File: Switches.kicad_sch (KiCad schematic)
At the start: 26 parts, among them J3 INDICATOR_SWITCH_OUT

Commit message: r pt 2
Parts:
- IGN_SW1: Height 15.1 -> (none); Manufacturer_Name C & K COMPONENTS -> (none); Manufacturer_Part_Number RM103772BCB -> (none); Mouser Part Number 611-RM103772BCB -> (none); Mouser Price/Stock https://www.mouser.co.uk/ProductDetail/CK/RM103772BCB?qs=36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 -> (none)
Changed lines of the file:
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@@
 			)
 		)
-		(property "Datasheet" "~"
+		(property "Datasheet" "https://www.ckswitches.com/media/1349/arotary.pdf"
 			(at 213.36 55.88 0)
 			(effects
@@
 			)
 		)
-		(property "Height" "15.1"
+		(property "Height" ""
 			(at 229.87 443.18 0)
 			(effects
@@
 			)
 		)
-		(property "Mouser Part Number" "611-RM103772BCB"
+		(property "Mouser Part Number" ""
 			(at 229.87 543.18 0)
 			(effects
@@
 			)
 		)
-		(property "Mouser Price/Stock" "https://www.mouser.co.uk/ProductDetail/CK/RM103772BCB?qs=367PjNmvCmkgg4M2NDGHLA%3D%3D"
+		(property "Mouser Price/Stock" ""
 			(at 229.87 643.18 0)
 			(effects
@@
 			)
 		)
-		(property "Manufacturer_Name" "C & K COMPONENTS"
+		(property "Manufacturer_Name" ""
 			(at 229.87 743.18 0)
 			(effects
@@
 			)
 		)
-		(property "Manufacturer_Part_Number" "RM103772BCB"
+		(property "Manufacturer_Part_Number" ""
 			(at 229.87 843.18 0)
 			(effects

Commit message: Changed layout, added 3d models
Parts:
- CRUZ_EN_SW1, CRUZ_SET_SW1: footprint switched:SW_Butt_) -> Button_Switch_THT:SW_PUSH_6mm
- GR_SW1: footprint switched:SW_100_SP3T-Vertical -> switched:3posSlideToggle
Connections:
- net +12V: now also GR_SW1.1; no longer GR_SW1.2 (3)
- net FWD_SW: now also GR_SW1.2; no longer GR_SW1.1
- net REV_SW: now also GR_SW1.4; no longer GR_SW1.3 (4)
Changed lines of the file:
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@@
 			)
 		)
-		(property "Footprint" "switched:SW_100_SP3T-Vertical"
+		(property "Footprint" "switched:3posSlideToggle"
 			(at 154.94 38.1 0)
 			(effects
@@
 			)
 		)
-		(property "Datasheet" "~"
+		(property "Datasheet" "https://www.vimex.com/switches/techdocs/SS13F11-tech.pdf"
 			(at 168.91 57.15 0)
 			(effects
@@
 		(pin "2"
 		)
-		(pin "3"
+		(pin "4"
 		)
 		(pin "1"
@@
 			)
 		)
-		(property "Footprint" "switched:SW_Butt_)"
+		(property "Footprint" "Button_Switch_THT:SW_PUSH_6mm"
 			(at 49.53 110.49 0)
 			(effects
@@
 			)
 		)
-		(property "Footprint" "switched:SW_Butt_)"
+		(property "Footprint" "Button_Switch_THT:SW_PUSH_6mm"
 			(at 86.36 110.49 0)
 			(effects

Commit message: Some extra stuff and things
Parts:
- HZD_SW1: symbol Switch:SW_SPST -> Switch:SW_Push
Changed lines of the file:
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@@
 	)
 	(symbol
-		(lib_id "Switch:SW_SPST")
+		(lib_id "Switch:SW_Push")
 		(at 109.22 45.72 270)
 		(unit 1)
@@
 		)
 		(property "Footprint" "switched:SW_HAZARD"
-			(at 109.22 45.72 0)
+			(at 114.3 45.72 0)
 			(effects
 				(font
@@
 			)
 		)
-		(property "Datasheet" "https://www.digikey.com/en/products/detail/switch-components/TE1-1A-DC-1-AL/11493057"
-			(at 109.22 45.72 0)
+		(property "Datasheet" "https://www.mouser.com/datasheet/2/140/P200001-2487714.pdf"
+			(at 114.3 45.72 0)
 			(effects
 				(font
@@
 			)
 		)
-		(property "Description" "Single Pole Single Throw (SPST) switch"
+		(property "Description" "Push button switch, generic, two pins"
 			(at 109.22 45.72 0)
 			(effects

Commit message: Fixed stuff
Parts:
- GR_SW1: Link (none) -> https://www.amazon.com/Yohii-Position-Vertical-Switch-SS13F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
- HZD_SW1: footprint switched:SW_HAZARD -> switched:Toggle; P/N (none) -> JN2UEENAGX
- IGN_SW1: DigiKey Part Number (none) -> CKN9823-ND; Manufacturer_Part_Number (none) -> A10305RNZQ
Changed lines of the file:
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@@
 			)
 		)
-		(property "Footprint" "switched:SW_HAZARD"
+		(property "Footprint" "switched:Toggle"
 			(at 114.3 45.72 0)
 			(effects
@@
 		(property "Description" "Push button switch, generic, two pins"
 			(at 109.22 45.72 0)
+			(effects
+				(font
+					(size 1.27 1.27)
+				)
+				(hide yes)
+			)
+		)
+		(property "P/N" "JN2UEENAGX"
+			(at 109.22 45.72 90)
 			(effects
 				(font
@@
 			)
 		)
+		(property "Link" "https://www.amazon.com/Yohii-Position-Vertical-Switch-SS13F11/dp/B07DNY27QB/ref=sr_1_1?crid=1IVIIMRQI2HJS&dib=eyJ2IjoiMSJ9.eq4ebiQlMkKEDFRAdhDxYwMIiYvkEjVZD_9xjgnfgCxXy-tZctG5FY5V9etNlcsO9SMg3hhRud0UZ8EvzB1QN5VE4UDG5s6WWWARvN8WRjMmnUkjLekKzcGdvc8ia7Sv9FLgmE0_jsopAeiuapqWnA.1wpn46VPwZhyZ5ITniFuaUG9biDjYCx3dxWY7euUJM8&dib_tag=se&keywords=SS13F11&qid=1732484796&sprefix=ss13f11%2Caps%2C110&sr=8-1"
+			(at 168.91 49.53 0)
+			(effects
+				(font
+					(size 1.27 1.27)
+				)
+				(hide yes)
+			)
+		)
 		(pin "2"
 		)
@@
 			)
 		)
-		(property "Mouser Part Number" ""
+		(property "DigiKey Part Number" "CKN9823-ND"
 			(at 229.87 543.18 0)
 			(effects
@@
 			)
 		)
-		(property "Mouser Price/Stock" ""
-			(at 229.87 643.18 0)
-			(effects
-				(font
-					(size 1.27 1.27)
-				)
-				(justify left top)
-				(hide yes)
-			)
-		)
-		(property "Manufacturer_Name" ""
-			(at 229.87 743.18 0)
-			(effects
-				(font
-					(size 1.27 1.27)
-				)
-				(justify left top)
-				(hide yes)
-			)
-		)
-		(property "Manufacturer_Part_Number" ""
+		(property "Manufacturer_Part_Number" "A10305RNZQ"
 			(at 229.87 843.18 0)
 			(effects
@@
 			)
 		)
-		(property "Datasheet" "https://switches-sensors.zf.com/wp-content/uploads/2024/10/kfb2ana1bbb.Rev_.H-1.pdf"
+		(property "Datasheet" ""
 			(at 49.53 110.49 0)
 			(effects
@@
 			)
 		)
-		(property "Datasheet" "https://switches-sensors.zf.com/wp-content/uploads/2024/10/kfb2ana1bbb.Rev_.H-1.pdf"
+		(property "Datasheet" ""
 			(at 86.36 110.49 0)
 			(effects

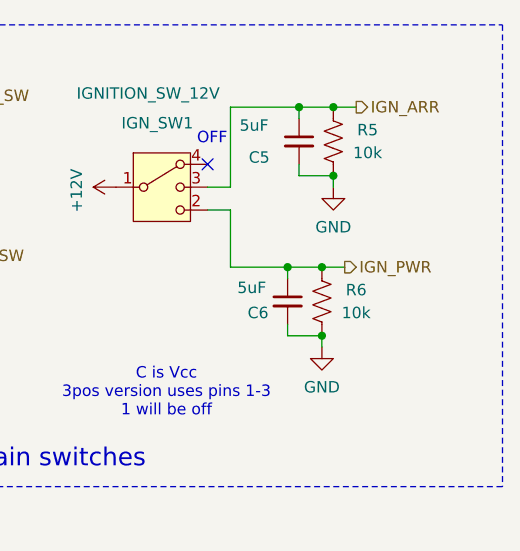
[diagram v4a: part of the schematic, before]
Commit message: Changed size and rerouted
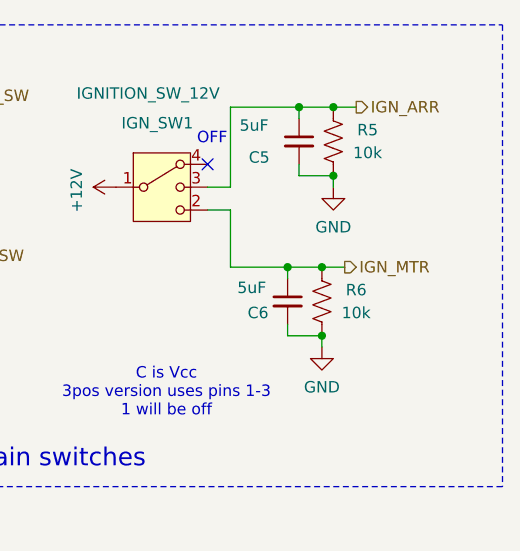
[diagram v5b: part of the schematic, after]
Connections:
- net IGN_PWR renamed IGN_MTR
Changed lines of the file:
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@@
 		)
 	)
-	(hierarchical_label "IGN_PWR"
+	(hierarchical_label "IGN_MTR"
 		(shape output)
 		(at 233.68 57.15 0)

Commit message: Final changes for now
added p/n n stuff
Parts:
- CRUZ_EN_SW1, CRUZ_SET_SW1: P/N (none) -> TS02-66-43-BK-100-LCR-D
- GR_SW1: P/N (none) -> SS13F11
- IGN_SW1: P/N (none) -> A10305RNZQ
- J3: P/N (none) -> 43650-0300

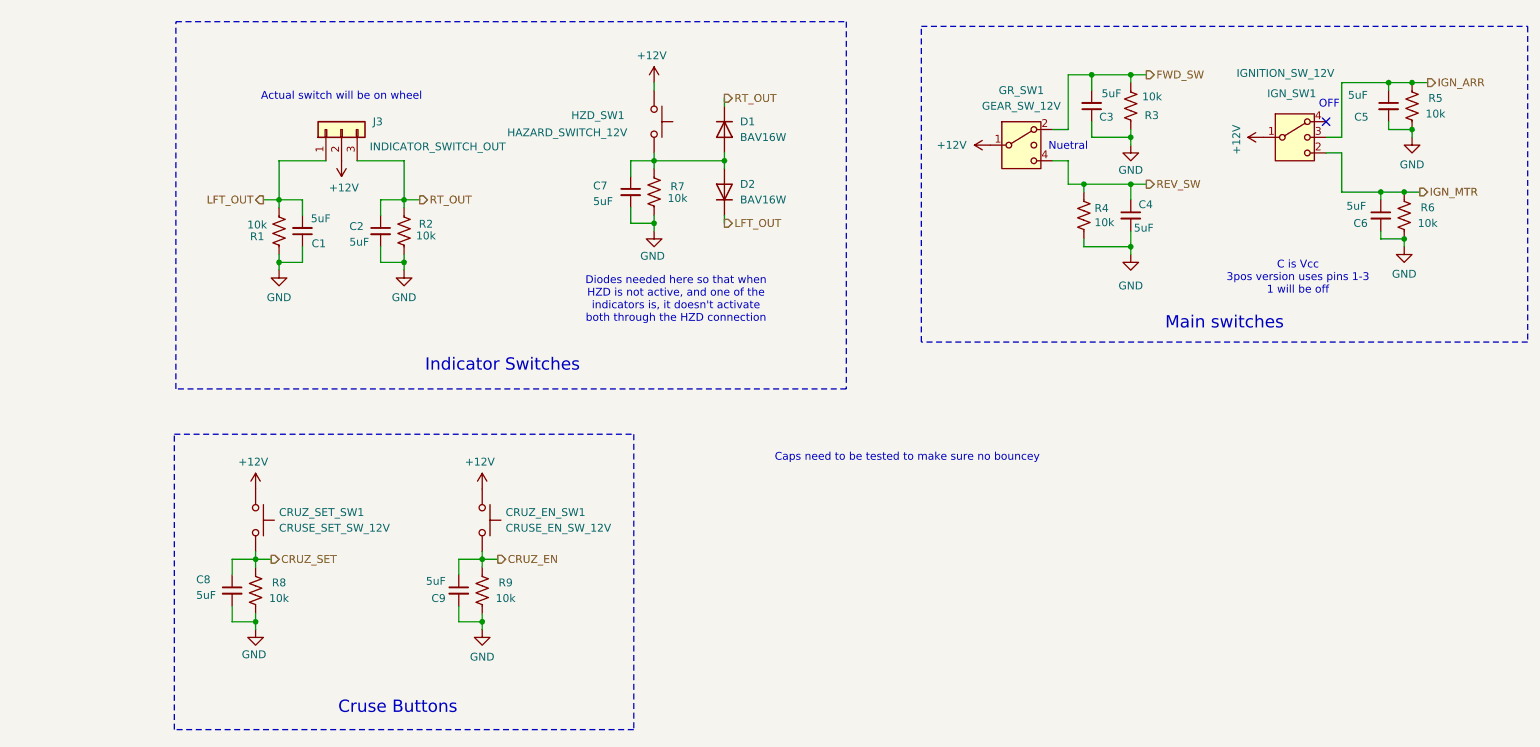
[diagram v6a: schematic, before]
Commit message: Delete submodule directory
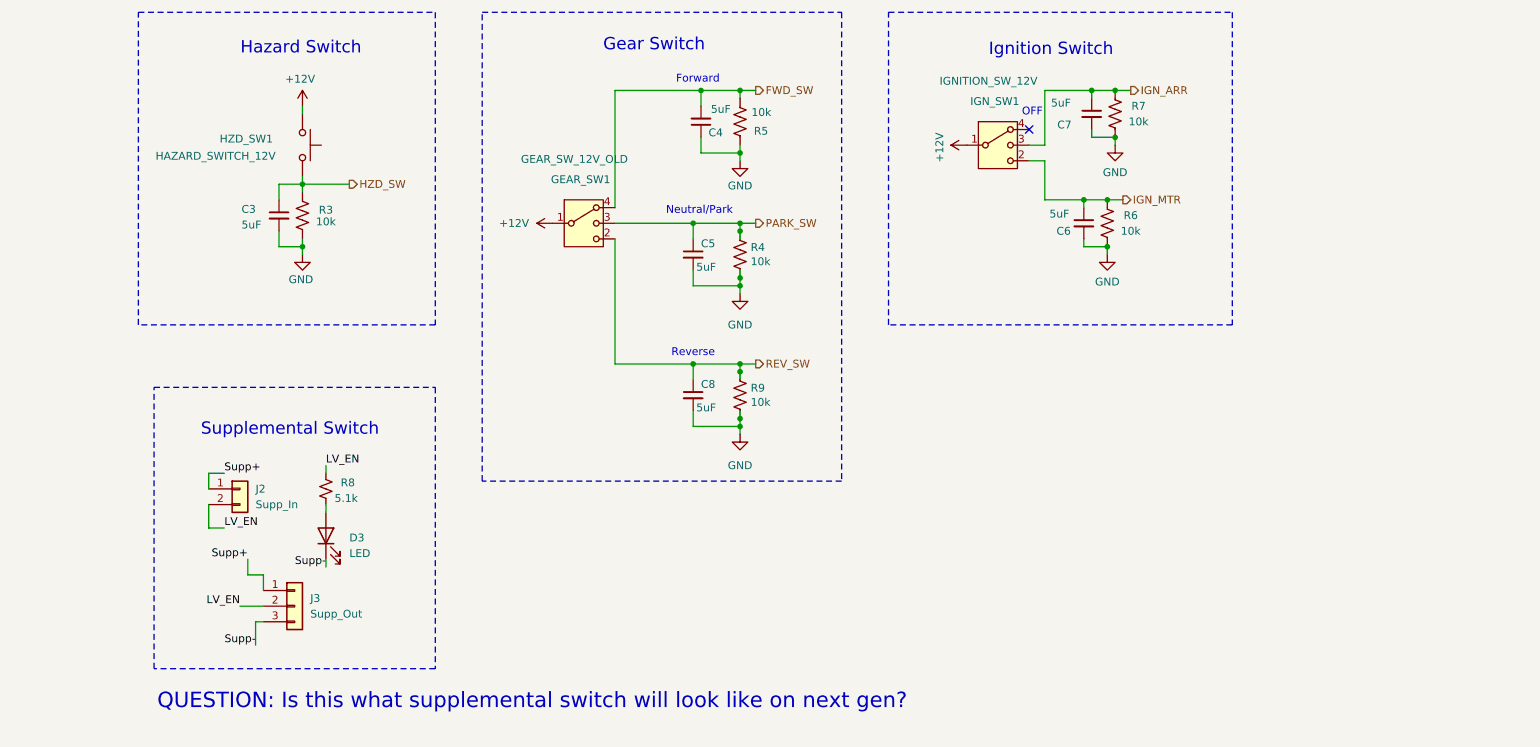
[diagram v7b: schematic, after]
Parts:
- removed C1, C2, C9: 5uF, Capacitor_SMD:C_0805_2012Metric, symbol Device:C_Small
- removed CRUZ_EN_SW1: CRUSE_EN_SW_12V, Button_Switch_THT:SW_PUSH_6mm, symbol Switch:SW_Push
- removed CRUZ_SET_SW1: CRUSE_SET_SW_12V, Button_Switch_THT:SW_PUSH_6mm, symbol Switch:SW_Push
- removed D1, D2: BAV16W, Diode_SMD:D_SOD-123, symbol Diode:BAV16W
- removed GR_SW1: GEAR_SW_12V, switched:3posSlideToggle, symbol Switch:SW_SPDT_MSM
- removed R1, R2, R8: 10k, Resistor_SMD:R_0805_2012Metric, symbol Device:R_US
- added D3: LED, LED_SMD:LED_0805_2012Metric, symbol Device:LED
- added GEAR_SW1: GEAR_SW_12V_OLD, switched:SW_3POS_ROT, symbol Switch:SW_SP3T
- added J2: Supp_In, Connector_Molex:Molex_Micro-Fit_3.0_43650-0215_1x02_P3.00mm_Vertical, symbol Connector_Generic:Conn_01x02
- added R8: 5.1k, Resistor_SMD:R_0805_2012Metric, symbol Device:R_Small_US
- J3: value INDICATOR_SWITCH_OUT -> Supp_Out
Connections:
- net CRUZ_EN is gone; now on net GND: R9.2
- net CRUZ_SET is gone; now on net REV_SW: C8.1
- net +12V: now also GEAR_SW1.1; no longer J3.2 (Pin_2)
- net FWD_SW: now also C4.2, R5.2, GEAR_SW1.4; no longer C3.2, R3.2
- net GND: now also C3.2, C4.1; no longer C3.1, C4.2, R9.1
- net IGN_ARR: now also C7.1, R7.2; no longer C5.1, R5.2
- net REV_SW: now also R9.1, GEAR_SW1.2; no longer C4.1, R4.1
- net LFT_OUT renamed Supp+
- net Supp+: now also J2.1 (Pin_1)
- net RT_OUT renamed Supp-
- net Supp-: now also D3.1 (K)
- new net: D3.2 (A), R8.2
- new net HZD_SW: C3.1, HZD_SW1.2, R3.2
- new net LV_EN: J2.2 (Pin_2), J3.2 (Pin_2), R8.1
- new net PARK_SW: C5.1, GEAR_SW1.3, R4.1
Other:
- note added: "Forward"
- note added: "Gear Switch"
- note added: "Hazard Switch"
- note added: "Ignition Switch"
- note added: "Neutral/Park"
- note added: "QUESTION: Is this what supplemental switch will look like on next gen?"
- note added: "Reverse"
- note added: "Supplemental Switch"
- note removed: "Actual switch will be on wheel"
- note removed: "C is Vcc 3pos version uses pins 1-3 1 will be off"
- note removed: "Caps need to be tested to make sure no bouncey"
- note removed: "Cruse Buttons"
- note removed: "Diodes needed here so that when HZD is not active, and one of the indicators is, it doesn't activate both through the HZD connection"
- note removed: "Indicator Switches"
- note removed: "Main switches"
- note removed: "Nuetral"

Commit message: Schematic updates. Ready for review, I think.
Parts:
- removed C7, C8: 5uF, Capacitor_SMD:C_0805_2012Metric, symbol Device:C_Small
- added C1, C2: 4.7uF, Capacitor_SMD:C_0805_2012Metric, symbol Device:C_Small
- added R1, R15: 6.04k, Resistor_SMD:R_0805_2012Metric, symbol Device:R_US
- added R14, R16, R2: 2k, Resistor_SMD:R_0805_2012Metric, symbol Device:R_US
- C3, C4, C5, C6: value 5uF -> 4.7uF; P/N C0805C103J5RACTU -> C0805C475K3RAC7210
- D3: value LED -> SMD_0805_YELLOW; P/N APTD2012LCGCK -> APTD2012LSYCK
- HZD_SW1: value HAZARD_SWITCH_12V -> HAZARD_SWITCH_3.3V
- J2: P/N 43650-0215 -> 436500215
- J3: P/N 43650-0300 -> 436500300
- R4, R5, R6: value 10k -> 6.04k; P/N CRCW080510K0FKEAC -> CRCW08056K04FKEA
- R7, R9: value 10k -> 2k; P/N CRCW080510K0FKEAC -> CRCW08052K00FKEAC
- R8: value 5.1k -> 4.7k; P/N CRCW0805100RFKEAHP -> CRCW08054K70FKEAC
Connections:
- net +12V: no longer HZD_SW1.1
- net FWD_SW: now also R5.1, R9.2; no longer C4.2, GEAR_SW1.4, R5.2
- net GND: now also C4.2, R9.1, C1.2, C2.2, R14.1, R16.1, R2.1; no longer C4.1, R4.2, R5.1, R6.1, R9.2
- net IGN_ARR: now also R14.2, R15.1; no longer IGN_SW1.3, R7.2
- net IGN_MTR: now also R6.1, R16.2; no longer C6.1, IGN_SW1.2, R6.2
- net PARK_SW: now also R7.2, R1.1; no longer C5.1, GEAR_SW1.3, R4.1
- net REV_SW: now also R4.1, R2.2; no longer GEAR_SW1.2, R9.1
- new net: C5.1, GEAR_SW1.2, R4.2
- new net: C6.1, IGN_SW1.2, R6.2
- new net: C2.1, GEAR_SW1.3, R1.2
- new net: C4.1, IGN_SW1.3, R15.2
- new net: C1.1, GEAR_SW1.4, R5.2
- new net +3.3V: HZD_SW1.1
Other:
- note added: "Park"
- note added: "Same supp switch connection as Daybreak supp"
- note removed: "Neutral/Park"
- note removed: "QUESTION: Is this what supplemental switch will look like on next gen?"
- moved on the sheet: D3, IGN_SW1, J2, J3, R8
